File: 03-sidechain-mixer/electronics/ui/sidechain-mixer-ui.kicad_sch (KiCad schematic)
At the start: 32 parts, among them J1 Conn_01x04, J2 Conn_02x05_Odd_Even, J3 Conn_02x03_Odd_Even, J4 Conn_01x02, J5 Conn_02x02_Counter_Clockwise, J6 Conn_01x06, U1 0203

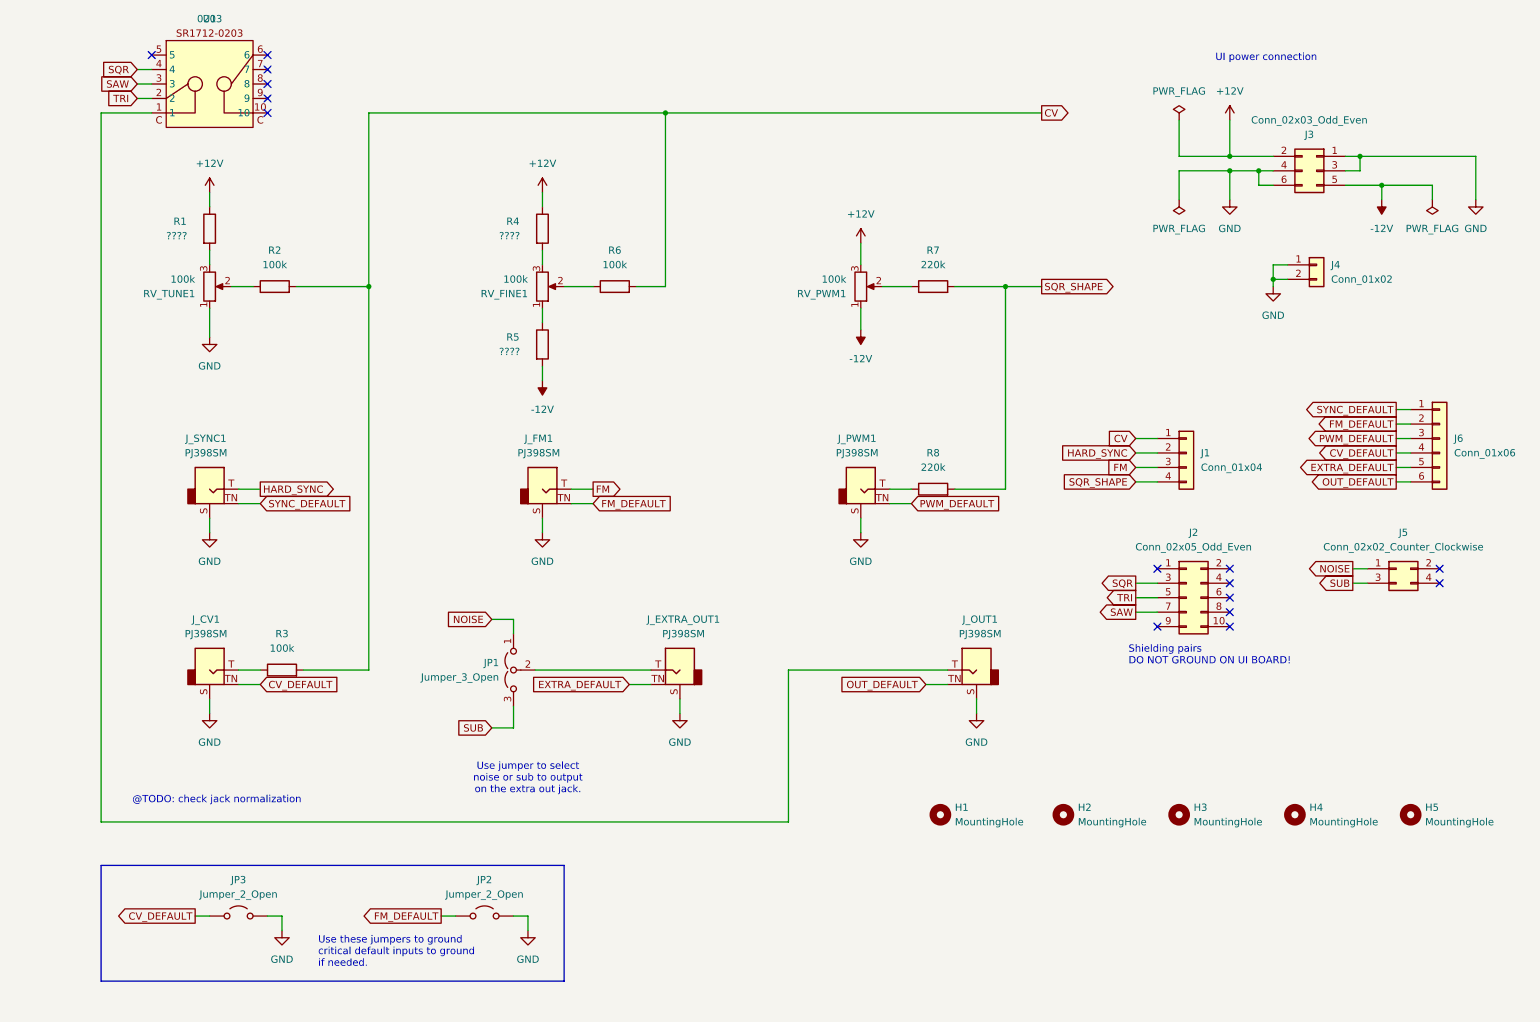
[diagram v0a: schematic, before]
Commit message: Added SC Mixer UI schematics
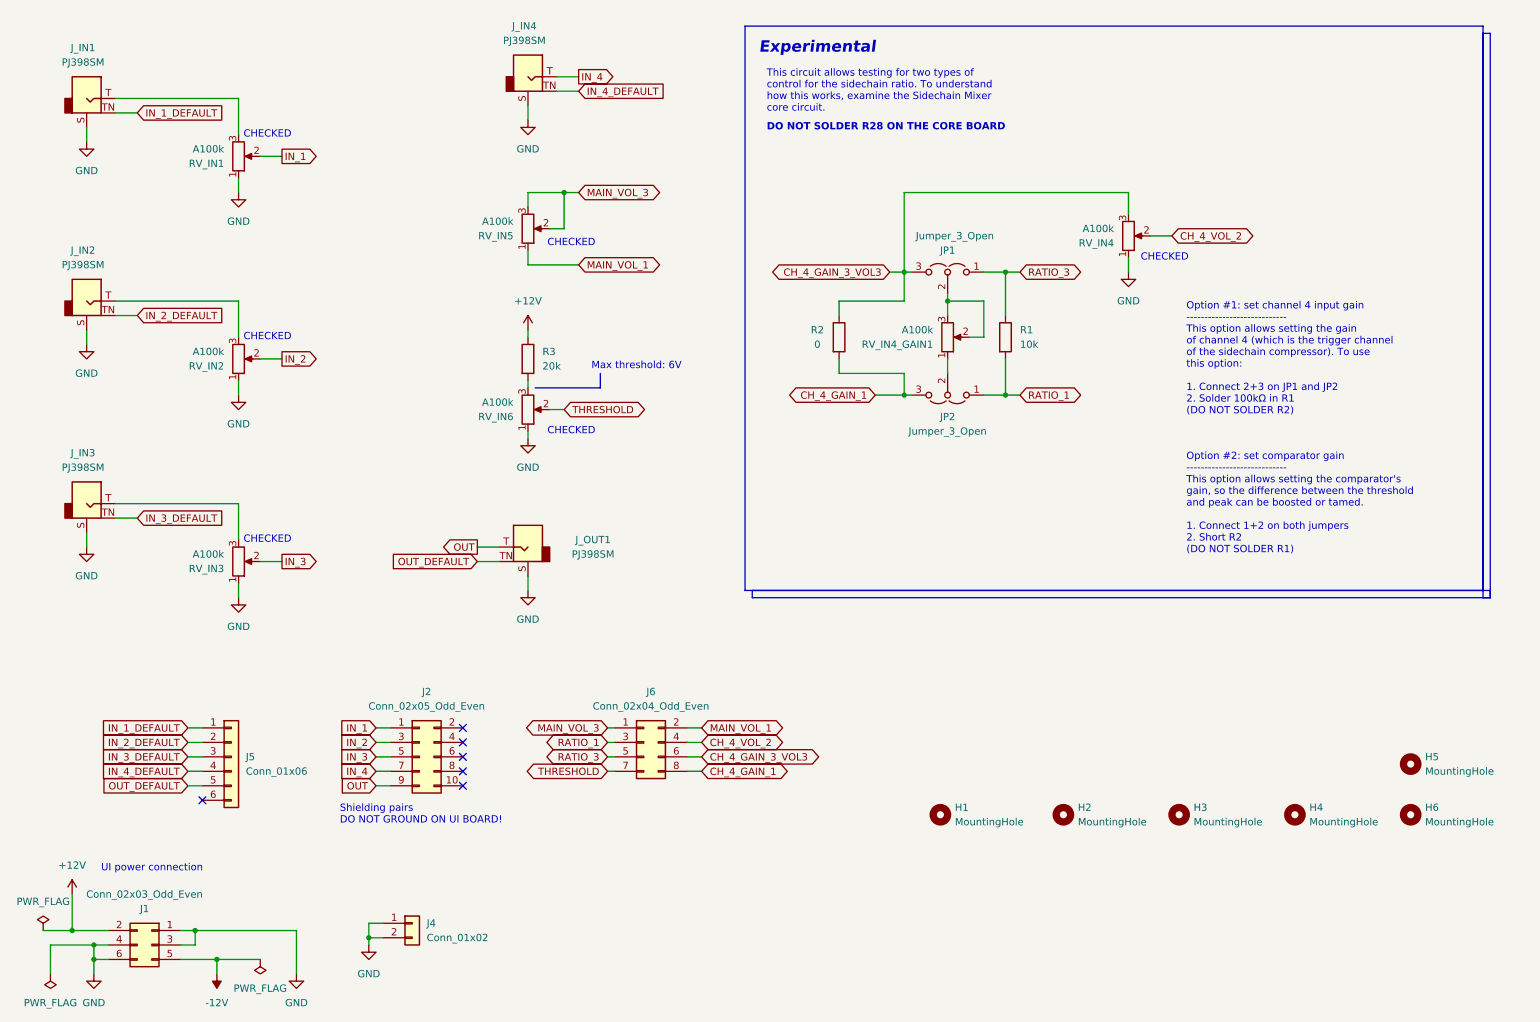
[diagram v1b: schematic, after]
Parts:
- removed J1: Conn_01x04, Connector_PinSocket_2.54mm:PinSocket_1x04_P2.54mm_Vertical, symbol Connector_Generic:Conn_01x04
- removed J5: Conn_02x02_Counter_Clockwise, Connector_PinSocket_2.54mm:PinSocket_2x02_P2.54mm_Vertical, symbol Connector_Generic:Conn_02x02_Odd_Even
- removed JP2, JP3: Jumper_2_Open, Connector_PinHeader_2.54mm:PinHeader_1x02_P2.54mm_Horizontal, symbol Jumper:Jumper_2_Open
- removed J_CV1, J_EXTRA_OUT1, J_FM1, J_PWM1: PJ398SM, Shmoergh_Custom_Footprints:Jack_3.5mm_QingPu_WQP-PJ398SM_Vertical_CircularHoles, symbol Shmoergh-Custom-Components:AudioJack2_Thonkiconn_S
- removed R4, R5: ????, Shmoergh_Custom_Footprints:R_Axial_DIN0207_L6.3mm_D2.5mm_P7.62mm_Horizontal, symbol Device:R
- removed R6: 100k, Shmoergh_Custom_Footprints:R_Axial_DIN0207_L6.3mm_D2.5mm_P7.62mm_Horizontal, symbol Device:R
- removed R7, R8: 220k, Shmoergh_Custom_Footprints:R_Axial_DIN0207_L6.3mm_D2.5mm_P7.62mm_Horizontal, symbol Device:R
- removed RV_FINE1, RV_PWM1, RV_TUNE1: 100k, Shmoergh_Custom_Footprints:Potentiometer_Bourns_Single-PTV09A, symbol Device:R_Potentiometer
- removed U1: 0203, Shmoergh_Custom_Footprints:SR1712-0203, symbol Shmoergh-Custom-Components:SR1712_0203
- added H5: MountingHole, MountingHole:MountingHole_3.2mm_M3_DIN965_Pad, symbol Mechanical:MountingHole
- added J6: Conn_02x04_Odd_Even, Connector_PinSocket_2.54mm:PinSocket_2x04_P2.54mm_Vertical, symbol Connector_Generic:Conn_02x04_Odd_Even
- added JP2: Jumper_3_Open, Connector_PinHeader_2.54mm:PinHeader_1x03_P2.54mm_Vertical, symbol Jumper:Jumper_3_Open
- added J_IN2, J_IN3, J_IN4: PJ398SM, Shmoergh_Custom_Footprints:Jack_3.5mm_QingPu_WQP-PJ398SM_Vertical_CircularHoles, symbol Shmoergh-Custom-Components:AudioJack2_Thonkiconn_S
- added RV_IN1, RV_IN2, RV_IN3, RV_IN4, RV_IN4_GAIN1, RV_IN5, RV_IN6: A100k, Shmoergh_Custom_Footprints:Potentiometer_Bourns_Single-PTV09A, symbol Device:R_Potentiometer
- J2: Part URL https://mou.sr/4lVCZM9 -> (none); Part no. 200-SSW10501TD -> (none); Vendor Mouser -> (none)
- JP1: footprint Connector_PinHeader_2.54mm:PinHeader_1x03_P2.54mm_Horizontal -> Connector_PinHeader_2.54mm:PinHeader_1x03_P2.54mm_Vertical; Part URL https://mou.sr/451l2py -> (none); Part no. 200-HTSW10308TSRA -> (none); Vendor Mouser -> (none); now left out of the parts list
- R1: value ???? -> 10k; Vendor Mouser -> (none)
- R2: value 100k -> 0; Part URL https://mou.sr/4hEwI4G -> (none); Part no. 603-MFR-25FRF52100K -> (none); Vendor Mouser -> (none)
- R3: value 100k -> 20k; Part URL https://mou.sr/4hEwI4G -> (none); Part no. 603-MFR-25FRF52100K -> (none); Vendor Mouser -> (none)
- renumbered H5 to H6, J3 to J1, J6 to J5, J_SYNC1 to J_IN1
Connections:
- net EXTRA_DEFAULT is gone; now on net OUT_DEFAULT: J5.5 (Pin_5)
- net SUB is gone; now on net CH_4_GAIN_3_VOL3: JP1.3 (B)
- net +12V: now also R3.1; no longer R1.1
- net GND: now also J_IN2.S, J_IN3.S, J_IN4.S, RV_IN1.1, RV_IN2.1, RV_IN3.1, RV_IN4.1, RV_IN6.1
- net OUT_DEFAULT: no longer J5.6 (Pin_6)
- net at JP1.2 (C): now also RV_IN4_GAIN1.2, RV_IN4_GAIN1.3
- net OUT: now reaches J_OUT1.T
- net OUT: now also J2.9 (Pin_9)
- net RATIO_1: now reaches R1.2
- net RATIO_1: now also J6.3 (Pin_3), JP2.1 (A)
- net IN_1: now reaches J2.1 (Pin_1)
- net IN_1: now also RV_IN1.2
- net CH_4_GAIN_3_VOL3: now reaches R2.1
- net CH_4_GAIN_3_VOL3: now also J6.6 (Pin_6), RV_IN4.3
- net CV: no longer names the net of R3.2
- net CV: now also RV_IN6.3; no longer R2.2
- net CV_DEFAULT renamed IN_4_DEFAULT
- net IN_4_DEFAULT: now also J_IN4.TN
- net FM_DEFAULT renamed IN_2_DEFAULT
- net IN_2_DEFAULT: now also J_IN2.TN
- net HARD_SYNC: no longer names the net of J_IN1.T
- net HARD_SYNC: now also RV_IN1.3
- net NOISE renamed RATIO_3
- net RATIO_3: now also R1.1, J6.5 (Pin_5)
- net PWM_DEFAULT renamed IN_3_DEFAULT
- net IN_3_DEFAULT: now also J_IN3.TN
- net SAW renamed IN_4
- net IN_4: now also J_IN4.T
- net SQR renamed IN_2
- net IN_2: now also RV_IN2.2
- net SYNC_DEFAULT renamed IN_1_DEFAULT
- net TRI renamed IN_3
- net IN_3: now also RV_IN3.2
- new net: JP2.2 (C), RV_IN4_GAIN1.1
- new net: J_IN2.T, RV_IN2.3
- new net: J_IN3.T, RV_IN3.3
- new net CH_4_GAIN_1: J6.8 (Pin_8), JP2.3 (B), R2.2
- new net CH_4_VOL_2: J6.4 (Pin_4), RV_IN4.2
- new net MAIN_VOL_1: J6.2 (Pin_2), RV_IN5.1
- new net MAIN_VOL_3: J6.1 (Pin_1), RV_IN5.2, RV_IN5.3
- new net THRESHOLD: J6.7 (Pin_7), RV_IN6.2
- no-connect marks 15 -> 6
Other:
- note added: "CHECKED"
- note added: "DO NOT SOLDER R28 ON THE CORE BOARD"
- note added: "Experimental"
- note added: "Max threshold: 6V"
- note added: "Option #1: set channel 4 input gain ---------------------------- This option allows setting the gain of channel 4 (which is the trigger channel of the sidechain compressor). To use this option: 1. Connect 2+3 on JP1 and JP2 2. Solder 100kΩ in R1 (DO NOT SOLDER R2)"
- note added: "Option #2: set comparator gain ---------------------------- This option allows setting the comparator's gain, so the difference between the threshold and peak can be boosted or tamed. 1. Connect 1+2 on both jumpers 2. Short R2 (DO NOT SOLDER R1)"
- note added: "This circuit allows testing for two types of control for the sidechain ratio. To understand how this works, examine the Sidechain Mixer core circuit."
- note removed: "@TODO: check jack normalization"
- note removed: "Use jumper to select noise or sub to output on the extra out jack."
- note removed: "Use these jumpers to ground critical default inputs to ground if needed."
- title: Hog Moduleur VCO UI -> Hog Moduleur Sidechain Mixer UI
- moved on the sheet: J1, J4, J5, J_IN1, J_OUT1

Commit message: Sidechain Mixer UI PCB RC
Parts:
- removed J6: Conn_02x04_Odd_Even, Connector_PinSocket_2.54mm:PinSocket_2x04_P2.54mm_Vertical, symbol Connector_Generic:Conn_02x04_Odd_Even
- added J3, J7: Conn_01x04, Connector_PinHeader_2.54mm:PinHeader_1x04_P2.54mm_Vertical, symbol Connector_Generic:Conn_01x04
- RV_IN1, RV_IN2, RV_IN3: footprint Shmoergh_Custom_Footprints:Potentiometer_Bourns_Single-PTV09A -> PTA3043-2010CIA503:TRIM_PTA3043-2010CIA503; Part URL https://mou.sr/4694GMU -> https://mou.sr/45jtvn7; Part no. 652-PTV09A4025FB104 -> 652-PTA30432015A104
- renumbered RV_IN5 to RV_MAIN_VOL1, RV_IN6 to RV_THRESHOLD1
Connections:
- net CH_4_GAIN_1: now also J7.3 (Pin_3)
- net CH_4_VOL_2: now also J7.2 (Pin_2)
- net MAIN_VOL_1: now also J7.1 (Pin_1)
- net MAIN_VOL_3: now also J3.1 (Pin_1)
- net RATIO_1: now also J3.2 (Pin_2)
- net RATIO_3: now also J3.3 (Pin_3)
- net THRESHOLD: now also J3.4 (Pin_4)
- net CH_4_GAIN_3_VOL3 renamed CH_4_GAIN_3_VOL_3
- net CH_4_GAIN_3_VOL_3: now also J7.4 (Pin_4)
